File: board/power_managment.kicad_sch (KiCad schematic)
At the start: 26 parts, among them U1 INA226AIDGSR, U1 XL7015E1, U3 AMS1117-3.3

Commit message: Hopefully finished schema for pcb
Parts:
- removed D2: TVS, symbol Device:D_Zener
- removed F3: Fuse, symbol Device:Fuse
- added D1: 1N53xxB, Diode_THT:D_DO-201_P15.24mm_Horizontal, symbol Diode:1N53xxB
- added D3: LED, symbol Device:LED
- added Q1: PMOS, symbol Simulation_SPICE:PMOS
- added R3: 100, symbol Device:R
- added R4: 10k, symbol Device:R
- added R6: 470, symbol Device:R
- added TVS1: SMAJ30CA, Diode_SMD:D_SMA, symbol Diode:SMAJ30CA
- H3: value BAT- -> BAT+ OUT
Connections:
- net 5+ SENSE IN: now also F1.2; no longer FB1.1
- net BAT+ SENSE IN: now also D1.1 (K), Q1.2 (G), Q1.3 (S), R3.1
- net GND: now also D3.1 (K), R4.2, TVS1.1 (A1)
- net at H1.1: now also Q1.1 (D), TVS1.2 (A2)
- net at C3.2, C4.1, C5.2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: now also F1.1; no longer FB1.2
- net 3V3 renamed +3V3
- net +3V3: now also FB1.1; no longer U3.2 (VO)
- net 5+ SENSE OUT renamed +5V
- net +5V: now also U3.3 (VI); no longer F1.1
- removed net 5V: F1.2, U3.3 (VI)
- new net: D1.2 (A), R3.2, R4.1
- new net: FB1.2, R6.1, U3.2 (VO)
- new net: D3.2 (A), R6.2
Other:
- note added: "Power in (TVS+Reverse polarity)"
- note removed: "Power in"
- moved on the sheet: C1, H2, U3

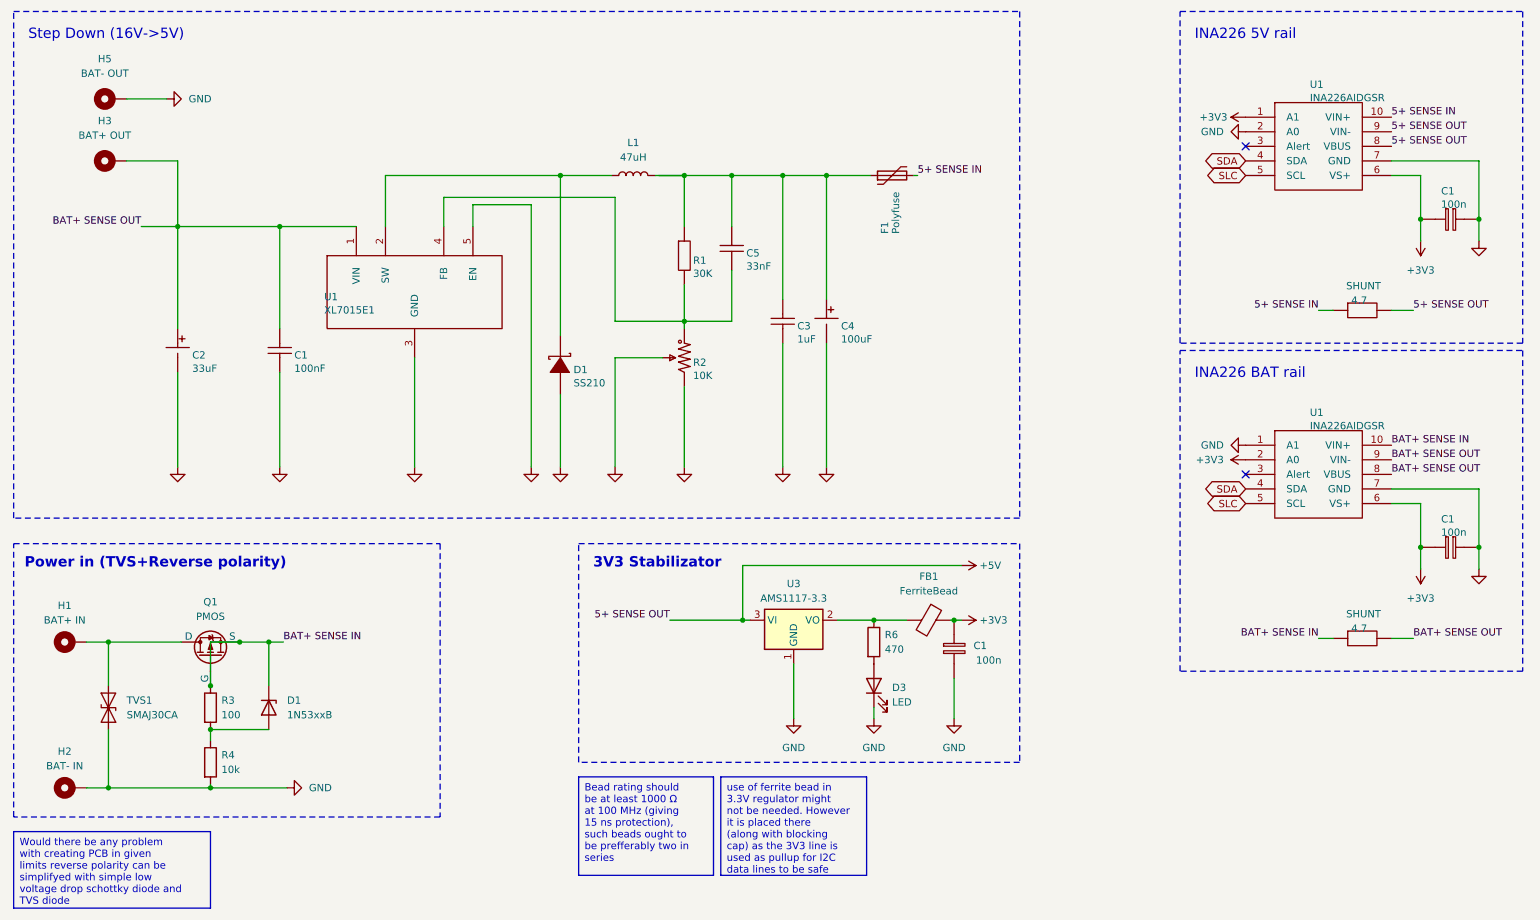
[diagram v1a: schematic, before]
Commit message: Updated schme to comply with electrical rules checker, prepared sensor logic for rewrite
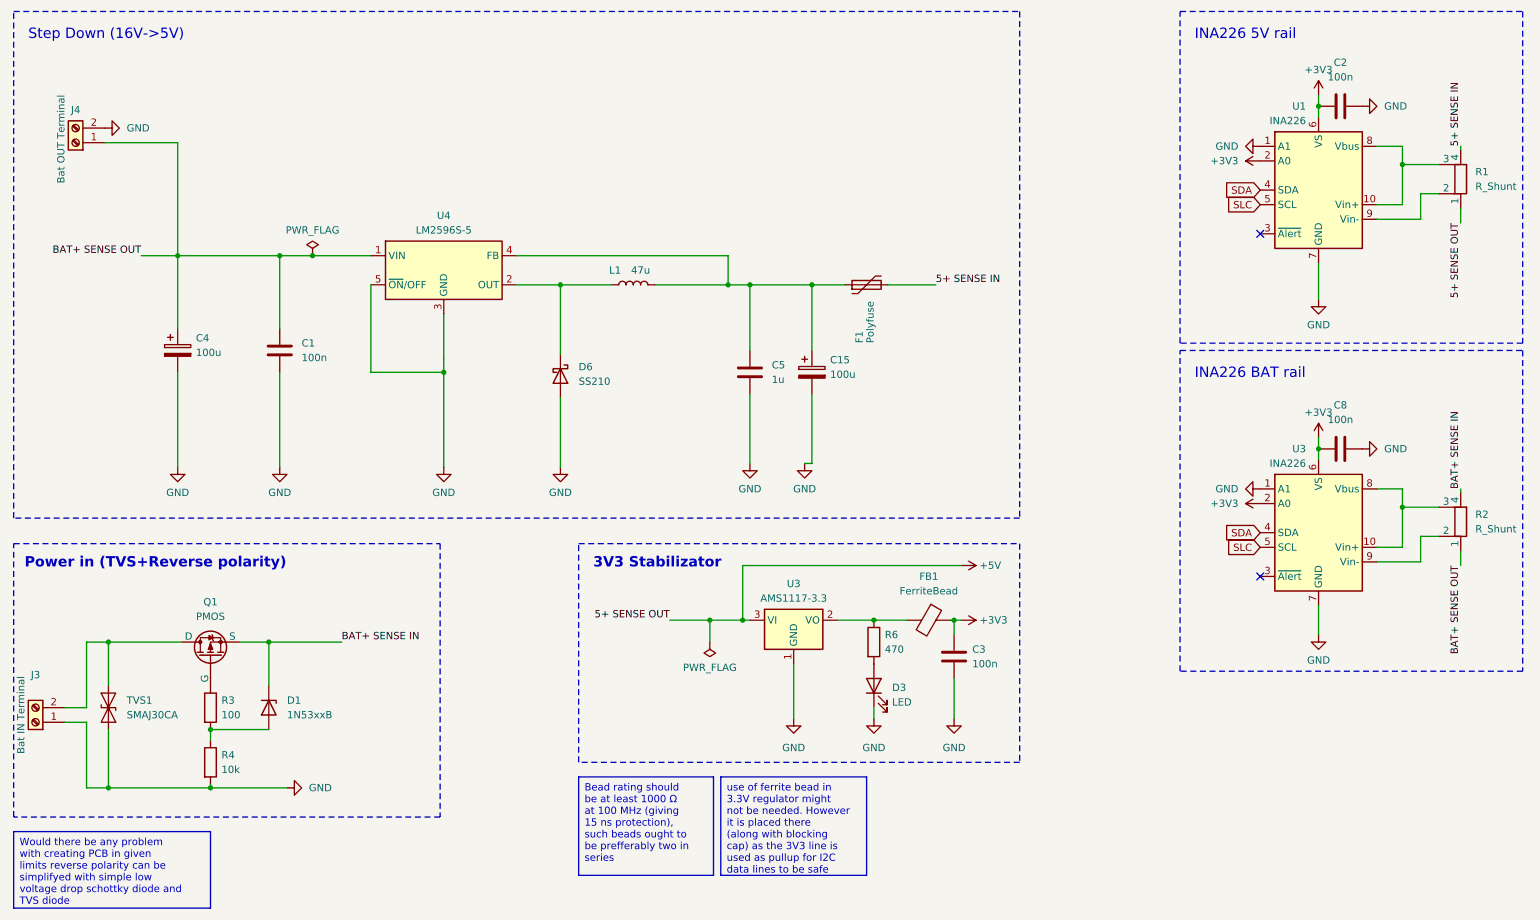
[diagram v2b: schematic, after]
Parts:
- removed C1 (x3): 100n, C0603, symbol SCH_ESP-12F Current Logger_2023-10-10:C_4B414481
- removed C1: 100nF, 0603, symbol SCH_Buck Converter_2023-10-10:C_4D7CDC59
- removed C2: 33uF, CAP-8*11.5, symbol SCH_Buck Converter_2023-10-10:C_FBF4E86A
- removed C3: 1uF, 0603, symbol SCH_Buck Converter_2023-10-10:C_4D7CDC59
- removed C4: 100uF, CAP-D6.3XF2.5, symbol SCH_Buck Converter_2023-10-10:C_6FAD636B
- removed C5: 33nF, 0603, symbol SCH_Buck Converter_2023-10-10:C_4D7CDC59
- removed D1: SS210, SMA(DO-214AC), symbol SCH_Buck Converter_2023-10-10:D_975584A9
- removed H1: BAT+ IN, symbol Mechanical:MountingHole_Pad
- removed H2: BAT- IN, symbol Mechanical:MountingHole_Pad
- removed H3: BAT+ OUT, symbol Mechanical:MountingHole_Pad
- removed H5: BAT- OUT, symbol Mechanical:MountingHole_Pad
- removed R1: 30K, 0402, symbol SCH_Buck Converter_2023-10-10:R_9356CC7C
- removed R2: 10K, RES-ADJ_3296W, symbol SCH_Buck Converter_2023-10-10:R_7ED27476
- removed SHUNT (x2): 4.7, R2512, symbol SCH_ESP-12F Current Logger_2023-10-10:R_2196C80A
- removed U1: XL7015E1, TO-252-5, symbol SCH_Buck Converter_2023-10-10:U_F5C12031
- removed U1 (x2): INA226AIDGSR, MSOP-10_L3.0-W3.0-P0.50-LS5.0-BL, symbol SCH_ESP-12F Current Logger_2023-10-10:U_7E3A5581
- added C1, C2, C3, C8: 100n, Capacitor_SMD:C_0603_1608Metric, symbol Device:C
- added C15: 100u, Capacitor_SMD:C_0402_1005Metric, symbol Device:C_Polarized
- added C4: 100u, symbol Device:C_Polarized
- added C5: 1u, symbol Device:C
- added D6: SS210, symbol Device:D_Schottky
- added J3: Bat IN Terminal, TerminalBlock:TerminalBlock_bornier-2_P5.08mm, symbol Connector:Screw_Terminal_01x02
- added J4: Bat OUT Terminal, TerminalBlock:TerminalBlock_bornier-2_P5.08mm, symbol Connector:Screw_Terminal_01x02
- added R1, R2: R_Shunt, symbol Device:R_Shunt
- added U1, U3: INA226, Package_SO:VSSOP-10_3x3mm_P0.5mm, symbol Sensor_Energy:INA226
- added U4: LM2596S-5, Package_TO_SOT_SMD:TO-263-5_TabPin3, symbol Regulator_Switching:LM2596S-5
- L1: value 47uH -> 47u; footprint (none) -> Inductor_SMD:L_0805_2012Metric
- R3, R4: footprint (none) -> Resistor_SMD:R_01005_0402Metric
- R6: footprint (none) -> Resistor_SMD:R_0603_1608Metric
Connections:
- net +3V3: now also C2.1, C3.1, C8.1, U1.2 (A0), U1.6 (VS), U3.2 (A0), U3.6 (VS)
- net +5V: now also R1.1
- net 5+ SENSE IN: now also R1.4
- net BAT+ SENSE IN: now also R2.4; no longer Q1.2 (G), R3.1
- net BAT+ SENSE OUT: now also C1.1, C4.1, J4.1 (Pin_1), R2.1, U4.1 (VIN)
- net GND: now also C1.2, C15.2, C2.2, C3.2, C4.2, C5.2, C8.2, D6.2 (A), J3.1 (Pin_1), J4.2 (Pin_2), U1.1 (A1), U1.7 (GND), U3.1 (A1), U3.7 (GND), U4.3 (GND), U4.5 (~{ON}/OFF)
- net SDA: now also U1.4 (SDA), U3.4 (SDA)
- net SLC: now also U1.5 (SCL), U3.5 (SCL)
- net at Q1.1 (D), TVS1.2 (A2): now also J3.2 (Pin_2)
- net at F1.1, L1.2: now also C15.1, C5.1, U4.4 (FB)
- net at L1.1: now also D6.1 (K), U4.2 (OUT)
- new net: Q1.2 (G), R3.1
- new net: R2.3, U3.10 (Vin+), U3.8 (Vbus)
- new net: R2.2, U3.9 (Vin-)
- new net: R1.2, U1.9 (Vin-)
- new net: R1.3, U1.10 (Vin+), U1.8 (Vbus)
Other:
- title: (none) -> Power supply and voltage monitoring
- moved on the sheet: F1, L1

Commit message: More work in reformating drone side of codebase to be semi usable
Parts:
- C15: footprint Capacitor_SMD:C_0402_1005Metric -> Capacitor_SMD:C_0603_1608Metric
- C4, C5: footprint (none) -> Capacitor_THT:CP_Radial_D8.0mm_P3.50mm
- D3: footprint (none) -> LED_SMD:LED_0805_2012Metric
- D6: footprint (none) -> Diode_SMD:D_SMB
- F1: footprint (none) -> Fuse:Fuse_1210_3225Metric
- FB1: footprint (none) -> Inductor_SMD:L_Ferrocore_DLG-0703
- L1: footprint Inductor_SMD:L_0805_2012Metric -> Inductor_SMD:L_12x12mm_H6mm
- Q1: footprint (none) -> Package_TO_SOT_THT:TO-220-3_Horizontal_TabDown
- R1, R2: footprint (none) -> Resistor_SMD:R_2512_6332Metric
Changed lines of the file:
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@@
+    )
+  )
+  (netclass_flag "" (length 2.54) (shape rectangle) (at 48.26 61.595 0)
+    (effects (font (size 1.27 1.27)) (justify left bottom))
+    (property "Netclass" "Battery" (at 50.165 59.055 0)
+      (effects (font (size 1.27 1.27) italic) (justify left))
     )
   )
@@
     )
   )
-  (netclass_flag "" (length 2.54) (shape round) (at 169.545 66.675 0) (fields_autoplaced)
-    (effects (font (size 1.27 1.27)) (justify left bottom))
-    (property "Netclass" "5V Line" (at 170.2435 64.135 0)
-      (effects (font (size 1.27 1.27) italic) (justify left))
-    )
-  )
   (netclass_flag "" (length 2.54) (shape round) (at 112.395 76.2 270) (fields_autoplaced)
     (effects (font (size 1.27 1.27)) (justify right bottom))
-    (property "Netclass" "5V Line" (at 114.935 75.5015 90)
-      (effects (font (size 1.27 1.27) italic) (justify left))
-    )
-  )
-  (netclass_flag "" (length 2.54) (shape rectangle) (at 49.53 61.595 0) (fields_autoplaced)
-    (effects (font (size 1.27 1.27)) (justify left bottom))
-    (property "Netclass" "Batter Line" (at 50.7365 59.055 0)
+    (property "Netclass" "+5V" (at 114.935 75.5015 90)
       (effects (font (size 1.27 1.27) italic) (justify left))
     )
@@
   (netclass_flag "" (length 2.54) (shape round) (at 134.62 61.595 0) (fields_autoplaced)
     (effects (font (size 1.27 1.27)) (justify left bottom))
-    (property "Netclass" "5V Line" (at 135.3185 59.055 0)
+    (property "Netclass" "+5V" (at 135.3185 59.055 0)
       (effects (font (size 1.27 1.27) italic) (justify left))
     )
@@
   (netclass_flag "" (length 2.54) (shape round) (at 182.245 125.095 0) (fields_autoplaced)
     (effects (font (size 1.27 1.27)) (justify left bottom))
-    (property "Netclass" "3V Line" (at 182.9435 122.555 0)
+    (property "Netclass" "+3V3" (at 182.9435 122.555 0)
       (effects (font (size 1.27 1.27) italic) (justify left))
     )
@@
   (netclass_flag "" (length 2.54) (shape rectangle) (at 33.655 128.905 0) (fields_autoplaced)
     (effects (font (size 1.27 1.27)) (justify left bottom))
-    (property "Netclass" "Batter Line" (at 34.8615 126.365 0)
+    (property "Netclass" "Battery" (at 34.8615 126.365 0)
       (effects (font (size 1.27 1.27) italic) (justify left))
     )
@@
   (netclass_flag "" (length 2.54) (shape round) (at 160.655 125.095 0) (fields_autoplaced)
     (effects (font (size 1.27 1.27)) (justify left bottom))
-    (property "Netclass" "3V Line" (at 161.3535 122.555 0)
+    (property "Netclass" "+3V3" (at 161.3535 122.555 0)
       (effects (font (size 1.27 1.27) italic) (justify left))
     )
@@
   (netclass_flag "" (length 2.54) (shape round) (at 147.32 115.57 0) (fields_autoplaced)
     (effects (font (size 1.27 1.27)) (justify left bottom))
-    (property "Netclass" "5V Line" (at 148.0185 113.03 0)
+    (property "Netclass" "+5V" (at 148.0185 113.03 0)
       (effects (font (size 1.27 1.27) italic) (justify left))
     )
@@
       (effects (font (size 1.27 1.27)) (justify left))
     )
-    (property "Footprint" "" (at 146.3802 85.725 0)
+    (property "Footprint" "Capacitor_THT:CP_Radial_D8.0mm_P3.50mm" (at 146.3802 85.725 0)
       (effects (font (size 1.27 1.27)) hide)
     )
@@
       (effects (font (size 1.27 1.27)))
     )
-    (property "Footprint" "" (at 176.53 123.317 90)
+    (property "Footprint" "Inductor_SMD:L_Ferrocore_DLG-0703" (at 176.53 123.317 90)
       (effects (font (size 1.27 1.27)) hide)
     )
@@
       (effects (font (size 1.27 1.27)) (justify right))
     )
-    (property "Footprint" "" (at 167.005 136.525 0)
+    (property "Footprint" "LED_SMD:LED_0805_2012Metric" (at 167.005 136.525 0)
       (effects (font (size 1.27 1.27)) hide)
     )
@@
       (effects (font (size 1.27 1.27)))
     )
-    (property "Footprint" "" (at 48.895 126.365 0)
+    (property "Footprint" "Package_TO_SOT_THT:TO-220-3_Horizontal_TabDown" (at 48.895 126.365 0)
       (effects (font (size 1.27 1.27)) hide)
     )
@@
       (effects (font (size 1.27 1.27)) (justify left))
     )
-    (property "Footprint" "" (at 112.395 82.55 0)
+    (property "Footprint" "Diode_SMD:D_SMB" (at 112.395 82.55 0)
       (effects (font (size 1.27 1.27)) hide)
     )
@@
       (effects (font (size 1.27 1.27)) (justify left))
     )
-    (property "Footprint" "Capacitor_SMD:C_0402_1005Metric" (at 157.1752 85.725 0)
+    (property "Footprint" "Capacitor_SMD:C_0603_1608Metric" (at 157.1752 85.725 0)
       (effects (font (size 1.27 1.27)) hide)
     )
@@
       (effects (font (size 1.27 1.27)) (justify left))
     )
-    (property "Footprint" "" (at 46.6852 81.915 0)
+    (property "Footprint" "Capacitor_THT:CP_Radial_D8.0mm_P3.50mm" (at 46.6852 81.915 0)
       (effects (font (size 1.27 1.27)) hide)
     )
@@
       (effects (font (size 1.27 1.27)))
     )
-    (property "Footprint" "Inductor_SMD:L_0805_2012Metric" (at 125.095 66.675 0)
+    (property "Footprint" "Inductor_SMD:L_12x12mm_H6mm" (at 125.095 66.675 0)
       (effects (font (size 1.27 1.27)) hide)
     )
@@
       (effects (font (size 1.27 1.27)) (justify right))
     )
-    (property "Footprint" "" (at 271.018 48.26 90)
+    (property "Footprint" "Resistor_SMD:R_2512_6332Metric" (at 271.018 48.26 90)
       (effects (font (size 1.27 1.27)) hide)
     )
@@
       (effects (font (size 1.27 1.27)) (justify right))
     )
-    (property "Footprint" "" (at 271.018 107.95 90)
+    (property "Footprint" "Resistor_SMD:R_2512_6332Metric" (at 271.018 107.95 90)
       (effects (font (size 1.27 1.27)) hide)
     )
@@
       (effects (font (size 1.27 1.27)) (justify left))
     )
-    (property "Footprint" "" (at 170.815 65.405 0)
+    (property "Footprint" "Fuse:Fuse_1210_3225Metric" (at 170.815 65.405 0)
       (effects (font (size 1.27 1.27)) (justify left) hide)
     )

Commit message: Started work on PCB design, more work on rewritting firmware to be semi usable
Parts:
- removed FB1: FerriteBead, Inductor_SMD:L_Ferrocore_DLG-0703, symbol Device:FerriteBead
- removed R1, R2: R_Shunt, Resistor_SMD:R_2512_6332Metric, symbol Device:R_Shunt
- added F1: Fuse, Fuse:Fuseholder_Clip-5x20mm_Littelfuse_111_Lateral_P18.80x5.00mm_D1.17mm_Horizontal, symbol Device:Fuse
- added R1, R2: 20m, Resistor_SMD:R_1210_3225Metric, symbol Device:R
- C1: footprint Capacitor_SMD:C_0603_1608Metric -> Diode_THT:D_DO-201_P12.70mm_Horizontal
- C5: value 1u -> 100n; footprint Capacitor_THT:CP_Radial_D8.0mm_P3.50mm -> Capacitor_SMD:C_0201_0603Metric
- D1: footprint Diode_THT:D_DO-201_P15.24mm_Horizontal -> Diode_THT:D_DO-201_P3.81mm_Vertical_AnodeUp
- L1: footprint Inductor_SMD:L_12x12mm_H6mm -> Inductor_SMD:L_7.3x7.3_H3.5
- Q1: footprint Package_TO_SOT_THT:TO-220-3_Horizontal_TabDown -> Package_TO_SOT_THT:TO-220-3_Vertical
- R3, R4: footprint Resistor_SMD:R_01005_0402Metric -> Resistor_SMD:R_1206_3216Metric
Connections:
- net 5+ SENSE IN is gone; now on net 5V SENSE IN: F1.2
- net BAT+ SENSE IN is gone; now on net BAT SENSE IN: D1.1 (K), Q1.3 (S)
- net BAT+ SENSE OUT is gone; now on net BAT SENSE OUT: C1.1, C4.1, J4.1 (Pin_1), U4.1 (VIN)
- net +3V3: now also R6.1, U3.2 (VO)
- net +5V: now also U1.8 (Vbus), U1.9 (Vin-), R1.2
- net GND: now also J3.2 (Pin_2); no longer J3.1 (Pin_1)
- net BAT UNSAFE: now reaches Q1.1 (D), TVS1.2 (A2)
- net BAT UNSAFE: now also J3.1 (Pin_1), F1.1, F1.2; no longer J3.2 (Pin_2)
- net BAT SENSE IN: now reaches U3.10 (Vin+)
- net BAT SENSE IN: now also R2.1; no longer U3.8 (Vbus)
- net BAT SENSE OUT: now reaches U3.9 (Vin-)
- net BAT SENSE OUT: now also U3.8 (Vbus), R2.2
- net 5V SENSE IN: now reaches U1.10 (Vin+)
- net 5V SENSE IN: now also R1.1; no longer U1.8 (Vbus)
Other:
- moved on the sheet: C3, J3
